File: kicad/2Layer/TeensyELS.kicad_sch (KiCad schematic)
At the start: 43 parts, among them J1 RJ45_Shielded, J2 Conn_01x04_Pin, J3 Conn_01x04_Pin, J4 Screw_Terminal_01x02, Q1 BSS138, Q2 BSS138, Q3 BSS138, Q4 BSS138, Q5 BSS138, Q6 BSS138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

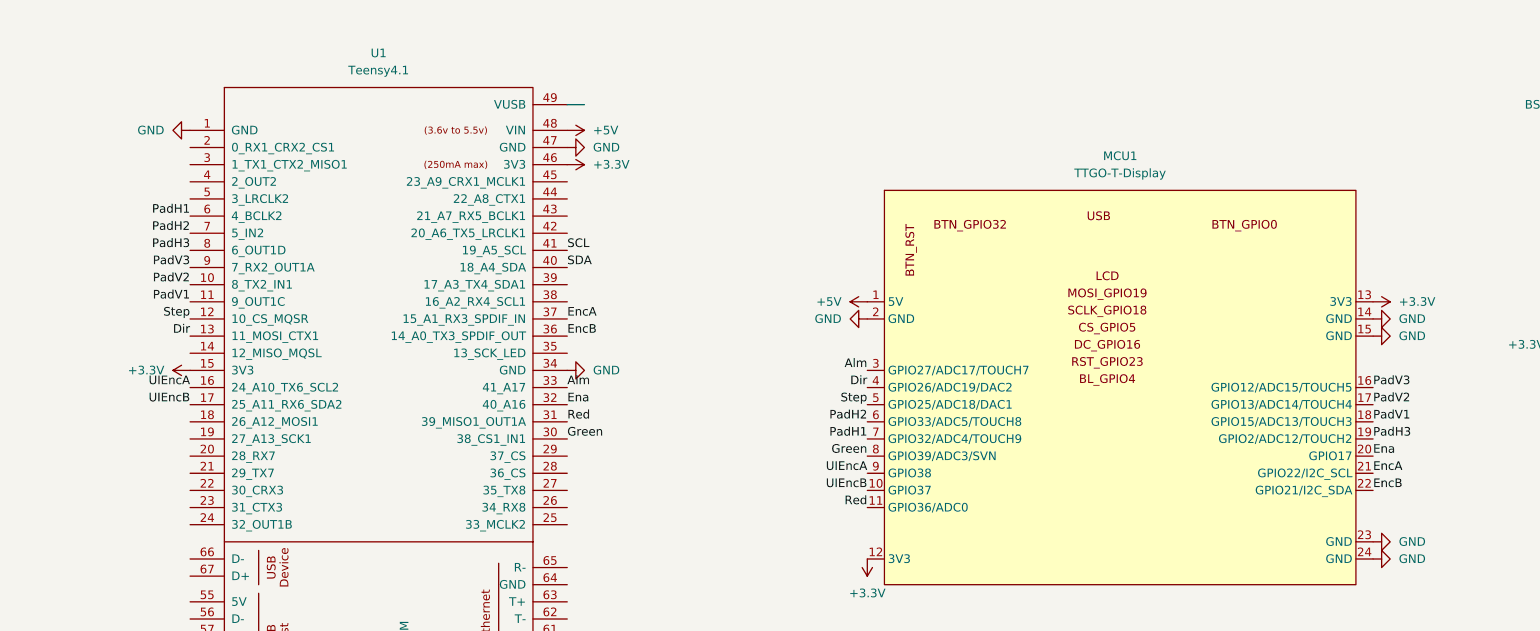
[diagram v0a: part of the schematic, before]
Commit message: Updated 2 layer designs
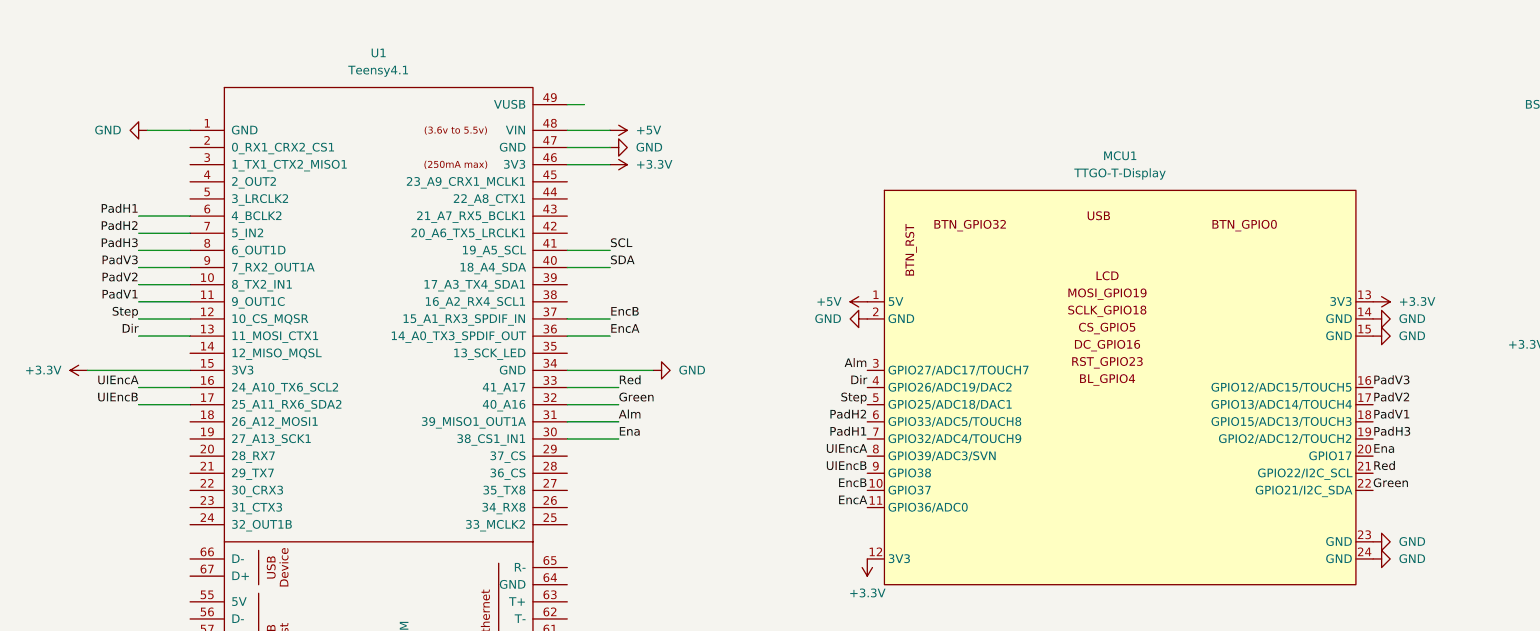
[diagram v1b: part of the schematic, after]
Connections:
- net Alm: now also U1.31 (39_MISO1_OUT1A); no longer U1.33 (41_A17)
- net Ena: now also U1.30 (38_CS1_IN1); no longer U1.32 (40_A16)
- net EncA: now also MCU1.11 (GPIO36/ADC0), U1.36 (14_A0_TX3_SPDIF_OUT); no longer MCU1.21 (GPIO22/I2C_SCL), U1.37 (15_A1_RX3_SPDIF_IN)
- net EncB: now also MCU1.10 (GPIO37), U1.37 (15_A1_RX3_SPDIF_IN); no longer MCU1.22 (GPIO21/I2C_SDA), U1.36 (14_A0_TX3_SPDIF_OUT)
- net Green: now also MCU1.22 (GPIO21/I2C_SDA), U1.32 (40_A16); no longer MCU1.8 (GPIO39/ADC3/SVN), U1.30 (38_CS1_IN1)
- net Red: now also MCU1.21 (GPIO22/I2C_SCL), U1.33 (41_A17); no longer MCU1.11 (GPIO36/ADC0), U1.31 (39_MISO1_OUT1A)
- net UIEncA: now also MCU1.8 (GPIO39/ADC3/SVN); no longer MCU1.9 (GPIO38)
- net UIEncB: now also MCU1.9 (GPIO38); no longer MCU1.10 (GPIO37)
